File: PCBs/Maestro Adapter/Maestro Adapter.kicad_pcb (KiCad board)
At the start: 2 copper layers, 51.4 x 45.8 mm, 20 parts

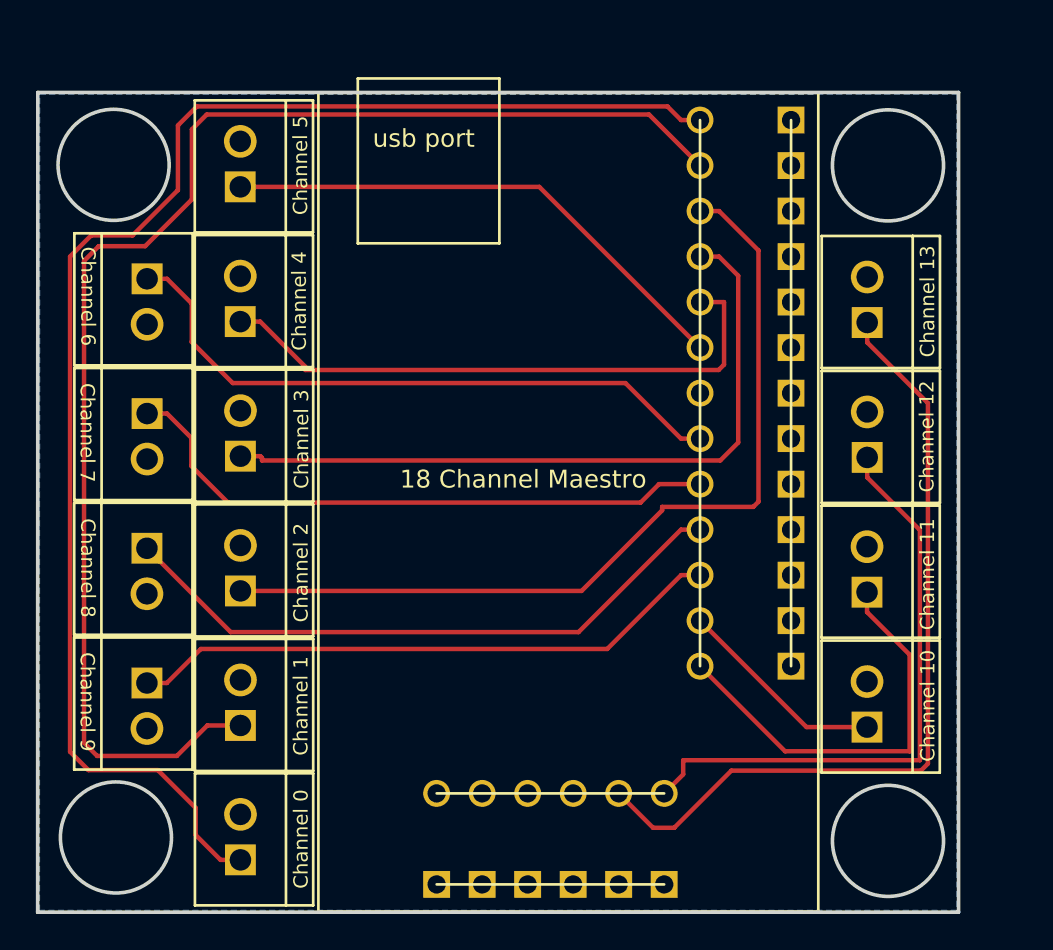
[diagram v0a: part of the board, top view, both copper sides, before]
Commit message: Changed the mounting holes
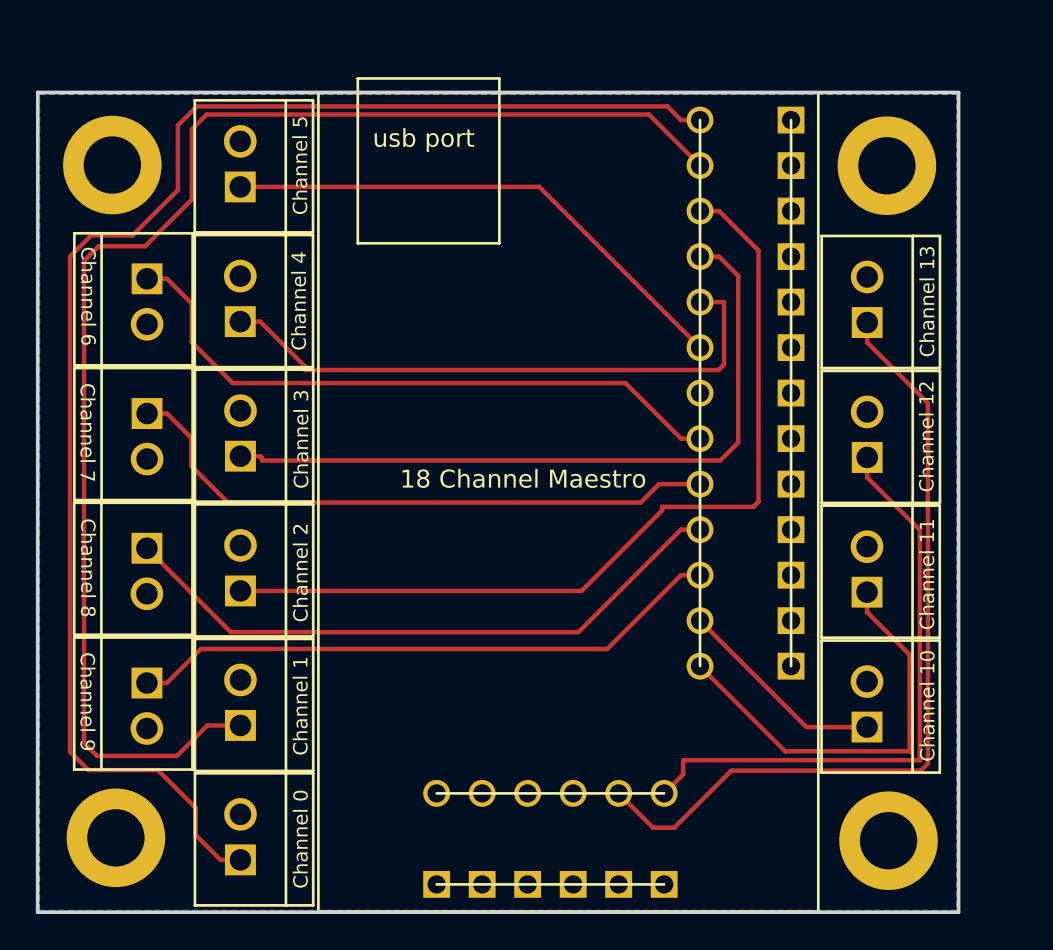
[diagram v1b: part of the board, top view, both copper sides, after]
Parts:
- added ?: , MountingHole:MountingHole_3.2mm_M3_ISO14580_Pad, F.Cu at (156.5, 83.3)
- added ?: , MountingHole:MountingHole_3.2mm_M3_ISO14580_Pad, F.Cu at (113.2, 83.3)
- added ?: , MountingHole:MountingHole_3.2mm_M3_ISO14580_Pad, F.Cu at (113.4, 120.8)
- added ?: , MountingHole:MountingHole_3.2mm_M3_ISO14580_Pad, F.Cu at (156.6, 121.0)
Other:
- outline, holes or cut-outs redrawn
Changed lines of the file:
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@@
-(kicad_pcb (version 20171130) (host pcbnew "(5.0.0)")
+(kicad_pcb (version 20171130) (host pcbnew "(5.0.1)-3")
   (general
     (thickness 1.6)
-    (drawings 8)
+    (drawings 4)
     (tracks 98)
     (zones 0)
-    (modules 20)
+    (modules 24)
     (nets 21)
   )
@@
     (mod_text_size 1 1)
     (mod_text_width 0.15)
-    (pad_size 1.524 1.524)
-    (pad_drill 0.762)
+    (pad_size 5.5 5.5)
+    (pad_drill 3.2)
     (pad_to_mask_clearance 0.051)
     (solder_mask_min_width 0.25)
@@
     (fp_poly (pts (xy 10.6125 -1.7125) (xy 10.6375 -1.7125) (xy 10.6375 -1.7375) (xy 10.6125 -1.7375)) (layer F.SilkS) (width 0))
   )
-  (gr_circle (center 156.52 120.98) (end 159.62 120.98) (layer Edge.Cuts) (width 0.2))
-  (gr_circle (center 156.52 83.28) (end 159.62 83.28) (layer Edge.Cuts) (width 0.2))
-  (gr_circle (center 113.3 83.25) (end 116.4 83.25) (layer Edge.Cuts) (width 0.2))
-  (gr_circle (center 113.43 120.79) (end 116.53 120.79) (layer Edge.Cuts) (width 0.2))
+  (module MountingHole:MountingHole_3.2mm_M3_ISO14580_Pad (layer F.Cu)
+    (at 156.46 83.3)
+    (descr "Mounting Hole 3.2mm, M3, ISO14580")
+    (tags "mounting hole 3.2mm m3 iso14580")
+    (attr virtual)
+    (fp_text reference "" (at 0 -3.75) (layer F.SilkS)
+      (effects (font (size 1 1) (thickness 0.15)))
+    )
+    (fp_text value "" (at 0 3.75) (layer F.Fab)
+      (effects (font (size 1 1) (thickness 0.15)))
+    )
+    (fp_circle (center 0 0) (end 3 0) (layer F.CrtYd) (width 0.05))
+    (fp_circle (center 0 0) (end 2.75 0) (layer Cmts.User) (width 0.15))
+    (fp_text user %R (at 0.3 0) (layer F.Fab)
+      (effects (font (size 1 1) (thickness 0.15)))
+    )
+    (pad "" thru_hole circle (at 0 0) (size 5.5 5.5) (drill 3.2) (layers *.Cu *.Mask))
+  )
+  (module MountingHole:MountingHole_3.2mm_M3_ISO14580_Pad (layer F.Cu)
+    (at 113.23 83.26)
+    (descr "Mounting Hole 3.2mm, M3, ISO14580")
+    (tags "mounting hole 3.2mm m3 iso14580")
+    (attr virtual)
+    (fp_text reference "" (at 0 -3.75) (layer F.SilkS)
+      (effects (font (size 1 1) (thickness 0.15)))
+    )
+    (fp_text value "" (at 0 3.75) (layer F.Fab)
+      (effects (font (size 1 1) (thickness 0.15)))
+    )
+    (fp_circle (center 0 0) (end 3 0) (layer F.CrtYd) (width 0.05))
+    (fp_circle (center 0 0) (end 2.75 0) (layer Cmts.User) (width 0.15))
+    (fp_text user %R (at 0.3 0) (layer F.Fab)
+      (effects (font (size 1 1) (thickness 0.15)))
+    )
+    (pad "" thru_hole circle (at 0 0) (size 5.5 5.5) (drill 3.2) (layers *.Cu *.Mask))
+  )
+  (module MountingHole:MountingHole_3.2mm_M3_ISO14580_Pad (layer F.Cu)
+    (at 113.43 120.81)
+    (descr "Mounting Hole 3.2mm, M3, ISO14580")
+    (tags "mounting hole 3.2mm m3 iso14580")
+    (attr virtual)
+    (fp_text reference "" (at 0 -3.75) (layer F.SilkS)
+      (effects (font (size 1 1) (thickness 0.15)))
+    )
+    (fp_text value "" (at 0 3.75) (layer F.Fab)
+      (effects (font (size 1 1) (thickness 0.15)))
+    )
+    (fp_circle (center 0 0) (end 3 0) (layer F.CrtYd) (width 0.05))
+    (fp_circle (center 0 0) (end 2.75 0) (layer Cmts.User) (width 0.15))
+    (fp_text user %R (at 0.3 0) (layer F.Fab)
+      (effects (font (size 1 1) (thickness 0.15)))
+    )
+    (pad "" thru_hole circle (at 0 0) (size 5.5 5.5) (drill 3.2) (layers *.Cu *.Mask))
+  )
+  (module MountingHole:MountingHole_3.2mm_M3_ISO14580_Pad (layer F.Cu)
+    (at 156.55 120.97)
+    (descr "Mounting Hole 3.2mm, M3, ISO14580")
+    (tags "mounting hole 3.2mm m3 iso14580")
+    (attr virtual)
+    (fp_text reference "" (at 0 -3.75) (layer F.SilkS)
+      (effects (font (size 1 1) (thickness 0.15)))
+    )
+    (fp_text value "" (at 0 3.75) (layer F.Fab)
+      (effects (font (size 1 1) (thickness 0.15)))
+    )
+    (fp_circle (center 0 0) (end 3 0) (layer F.CrtYd) (width 0.05))
+    (fp_circle (center 0 0) (end 2.75 0) (layer Cmts.User) (width 0.15))
+    (fp_text user %R (at 0.3 0) (layer F.Fab)
+      (effects (font (size 1 1) (thickness 0.15)))
+    )
+    (pad "" thru_hole circle (at 0 0) (size 5.5 5.5) (drill 3.2) (layers *.Cu *.Mask))
+  )
   (gr_line (start 109.06 124.96) (end 109.07 79.21) (layer Edge.Cuts) (width 0.2))
   (gr_line (start 160.46 124.96) (end 109.06 124.96) (layer Edge.Cuts) (width 0.2))

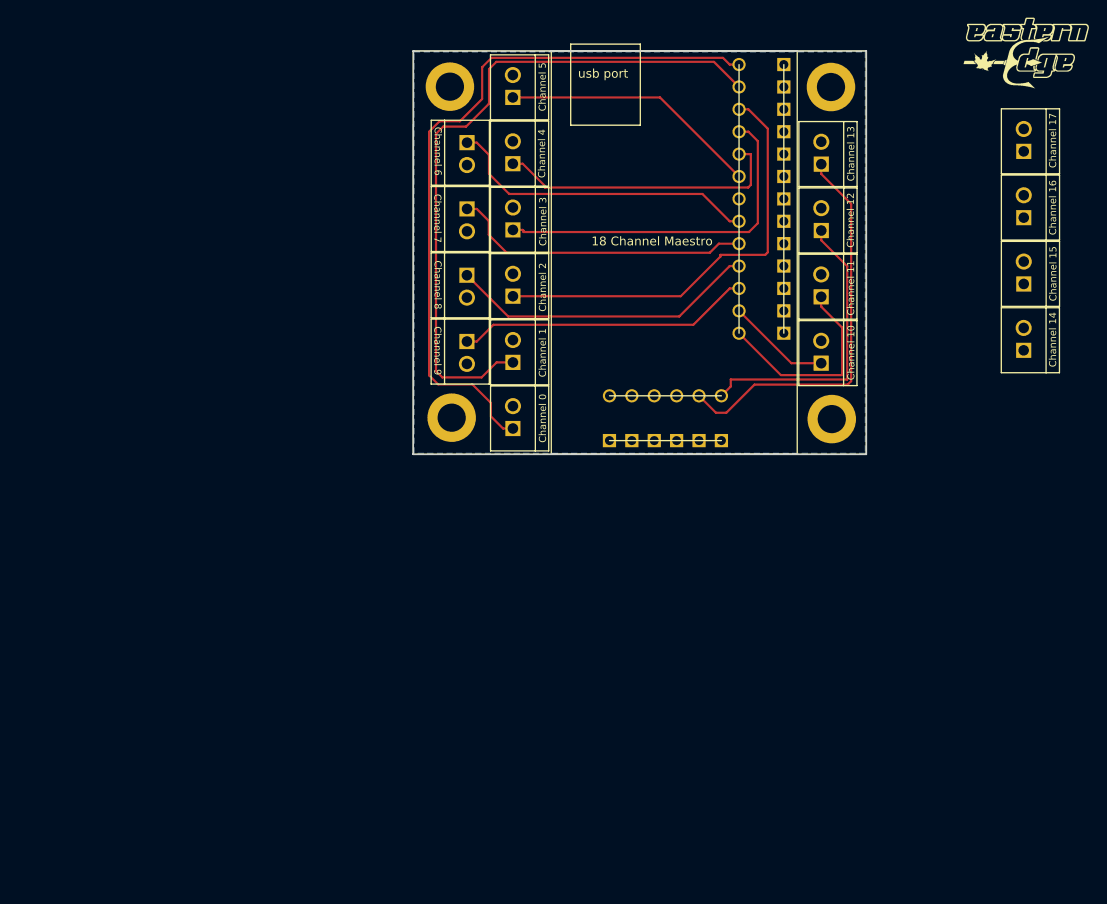
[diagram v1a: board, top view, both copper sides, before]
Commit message: Move maestro to the bottom and move connectors
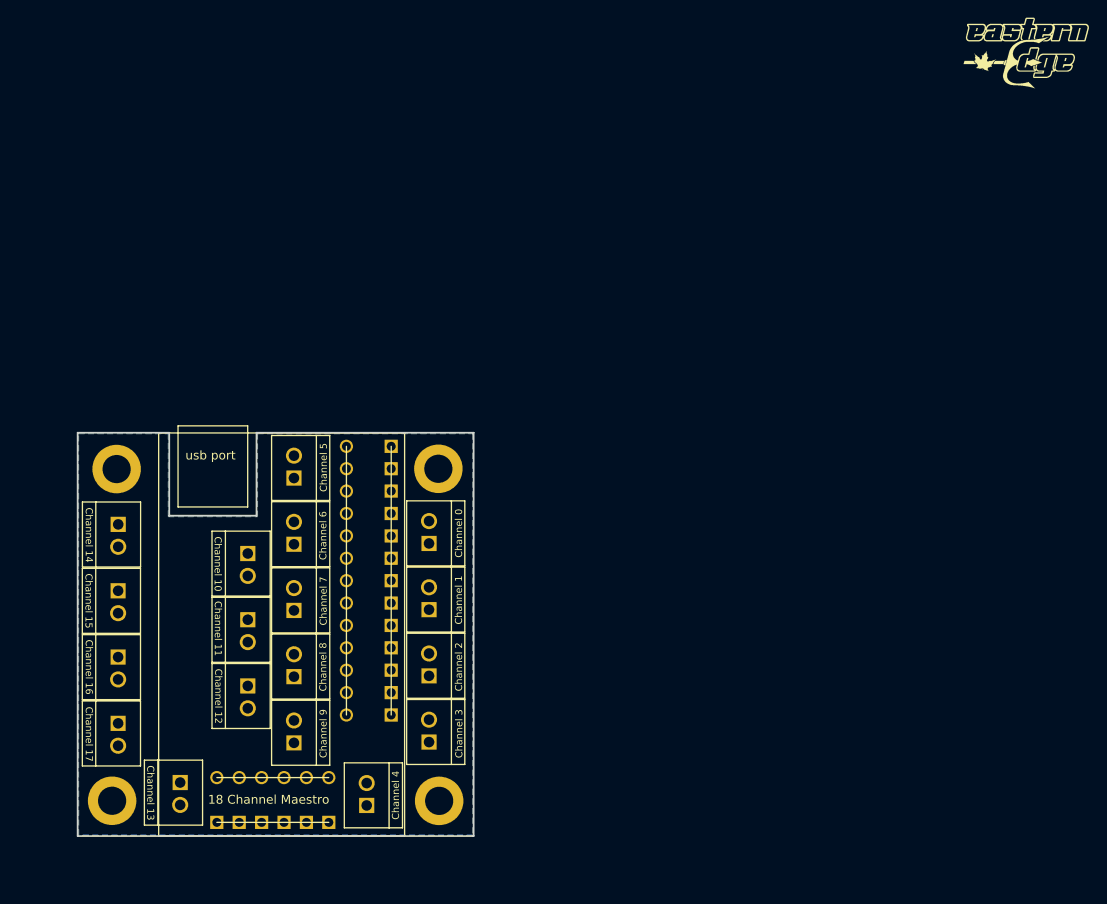
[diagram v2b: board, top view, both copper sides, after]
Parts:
- moved Channel 17 114.5 mm to (78.1, 152.9), turned to 180 degrees
- moved Channel 16 107.4 mm to (78.1, 145.4), turned to 180 degrees
- moved Channel 15 102.1 mm to (78.1, 137.9), turned to 180 degrees
- moved Channel 14 98.7 mm to (78.1, 130.4), turned to 180 degrees
- moved Channel 13 93.9 mm to (85.2, 159.7), turned to 180 degrees
- moved Channel 12 75.9 mm to (92.8, 148.7), turned to 180 degrees
- moved Channel 4 74.7 mm to (101.2, 167.3)
- moved Channel 11 67.8 mm to (92.8, 141.2), turned to 180 degrees
- moved Channel 10 62.2 mm to (92.8, 133.7), turned to 180 degrees
- moved 18 Channel Maestro 62.1 mm to (80.2, 168.2)
- moved ? 62.1 mm to (111.9, 126.6)
- moved ? 62.1 mm to (112.0, 164.3)
- moved Channel 3 58.9 mm to (108.3, 160.2)
- moved ? 58.1 mm to (74.9, 164.3)
- moved ? 57.5 mm to (75.4, 126.6)
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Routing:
- net Net-(J0-Pad1): track 81.6 -> 0.00 mm
- net Net-(J1-Pad1): track 77.9 -> 0.00 mm
- net Net-(J18-Pad3): track 49.3 -> 0.00 mm
- net Net-(J13-Pad1): track 45.6 -> 0.00 mm
- net Net-(J18-Pad4): track 40.3 -> 0.00 mm
- net Net-(J18-Pad8): track 35.8 -> 0.00 mm
- net Net-(J18-Pad10): track 35.2 -> 0.00 mm
- net Net-(J18-Pad9): track 34.3 -> 0.00 mm
- net Net-(J12-Pad1): track 33.6 -> 0.00 mm
- net Net-(J18-Pad11): track 33.4 -> 0.00 mm
- net Net-(J18-Pad5): track 33.2 -> 0.00 mm
- net Net-(J18-Pad6): track 29.4 -> 0.00 mm
- net Net-(J11-Pad1): track 23.5 -> 0.00 mm
- net Net-(J10-Pad1): track 11.8 -> 0.00 mm
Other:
- board size 51.4 x 45.8 mm -> 44.9 x 45.8 mm

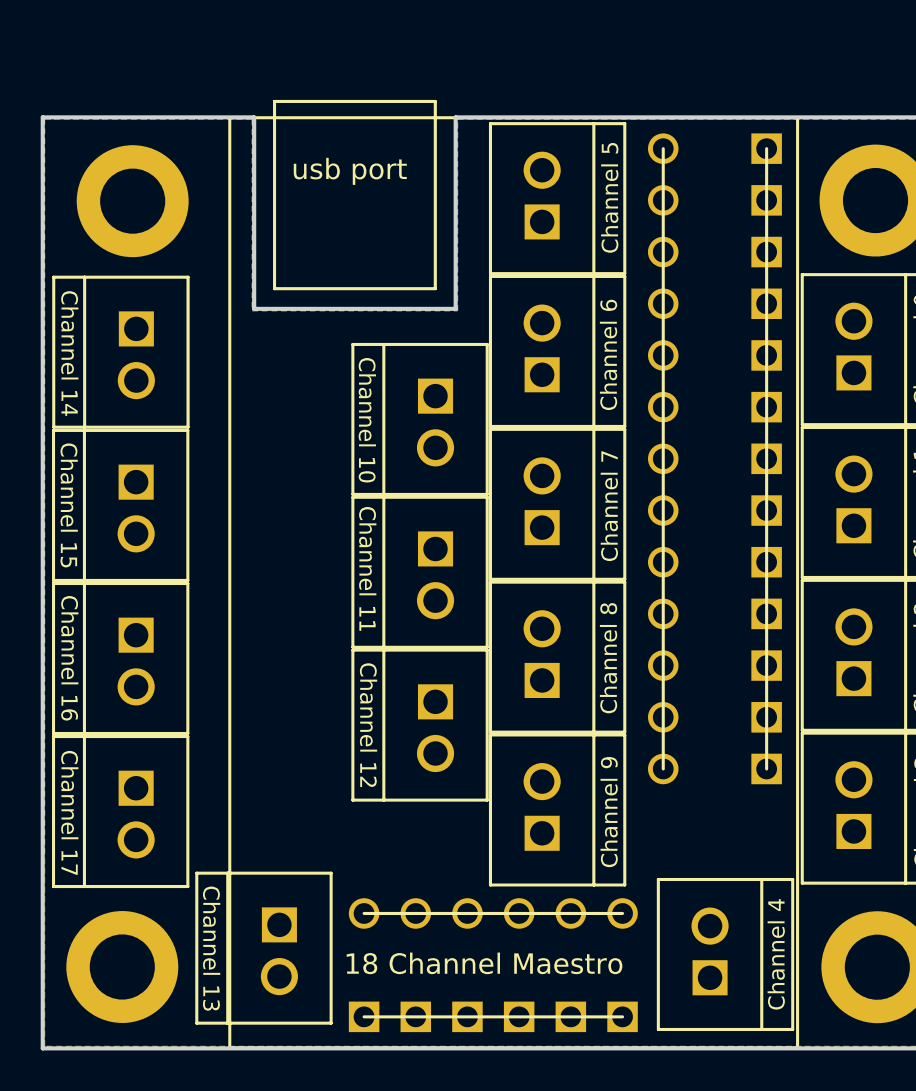
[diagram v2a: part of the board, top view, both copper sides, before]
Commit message: rearanged connectors and updated footprint with new 3d model path
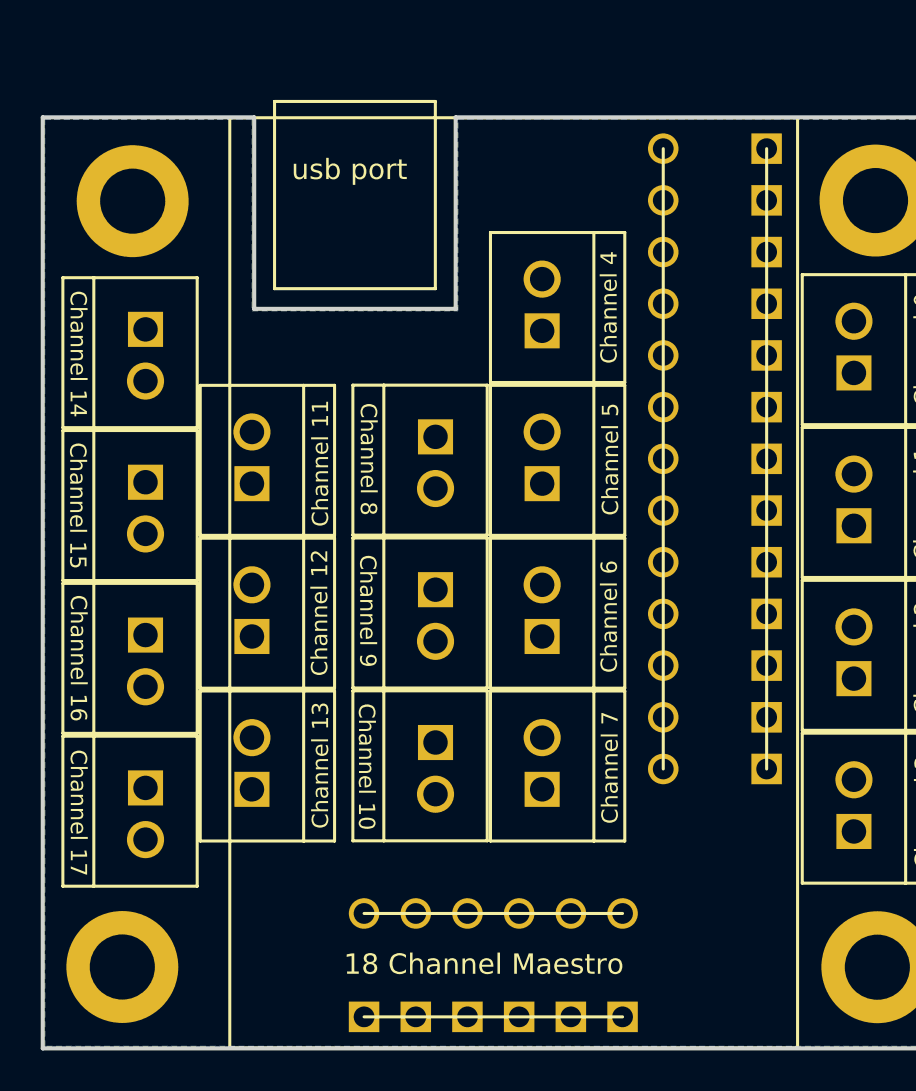
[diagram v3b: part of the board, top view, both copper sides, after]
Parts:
- moved Channel 4 32.8 mm to (93.0, 135.6)
- moved Channel 9 17.1 mm to (92.8, 143.2), turned to 180 degrees
- moved Channel 8 17.1 mm to (92.8, 135.7), turned to 180 degrees
- moved Channel 10 17.0 mm to (92.8, 150.7)
- moved Channel 11 14.2 mm to (78.7, 143.1), turned to 0 degrees
- moved Channel 12 14.2 mm to (78.7, 150.6), turned to 0 degrees
- moved Channel 5 12.9 mm to (93.0, 143.1)
- moved Channel 7 12.9 mm to (93.0, 158.1)
- moved Channel 6 12.9 mm to (93.0, 150.6)
- moved Channel 13 6.62 mm to (78.7, 158.1), turned to 0 degrees
- moved Channel 17 0.46 mm to (78.6, 152.9)
- moved Channel 16 0.46 mm to (78.6, 145.4)
- moved Channel 15 0.46 mm to (78.6, 137.9)
- moved Channel 14 0.45 mm to (78.6, 130.4)
